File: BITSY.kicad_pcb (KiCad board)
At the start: 4 copper layers, 102 x 102 mm, 64 parts, among them CON1 AudioJack3_SwitchTR, J1 Barrel_Jack_Switch, J2 Conn_01x06, J3 Conn_01x05, J4 Conn_02x22_Odd_Even, J5 Conn_01x40_Pin, J6 Conn_01x01_Socket, J7 Conn_01x01_Socket, J8 Conn_01x01_Socket, J9 Conn_01x01_Socket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

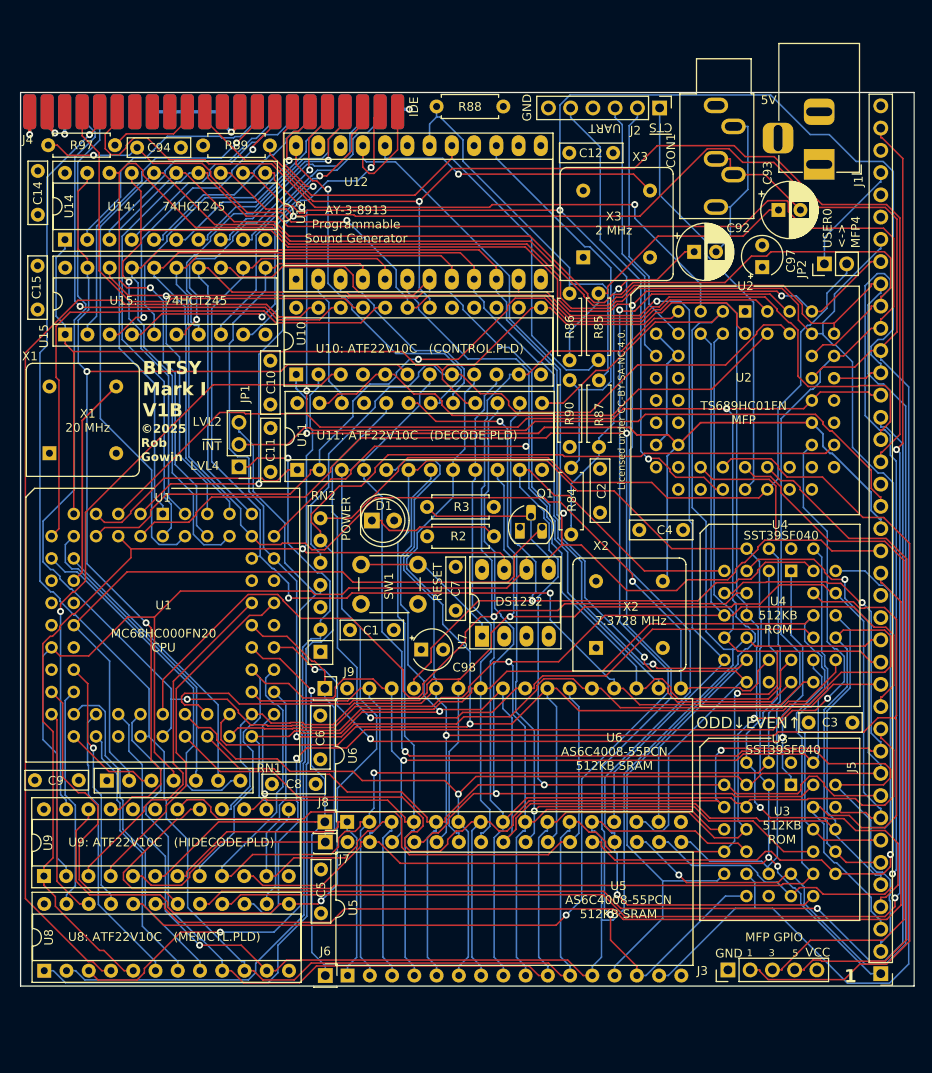
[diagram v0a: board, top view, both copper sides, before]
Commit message: V1C version of BITSY that uses an SRAM SIMM for memory.
This version sent to JLCPCB on 08/15/2025.
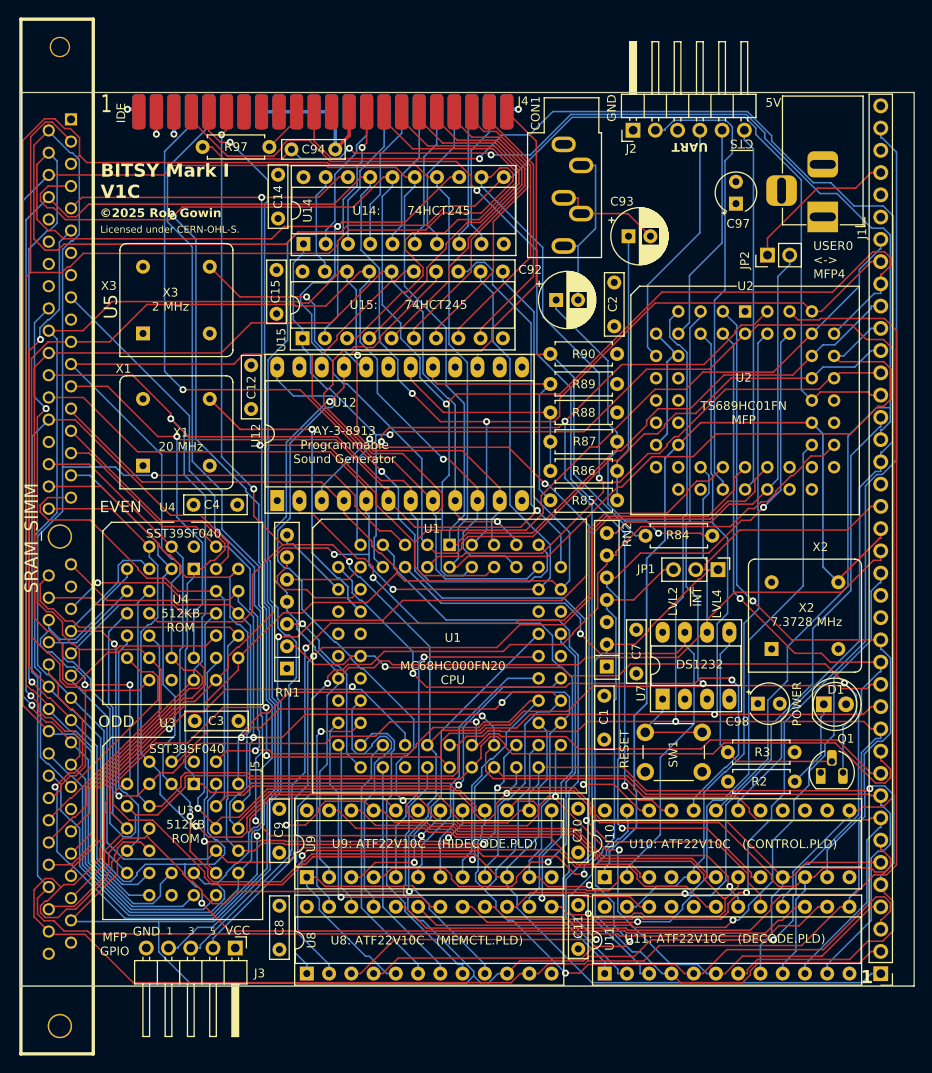
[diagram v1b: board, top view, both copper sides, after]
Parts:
- removed C5, C6: 0.1uF, Capacitor_THT:C_Rect_L7.0mm_W2.0mm_P5.00mm
- removed J6, J7, J8, J9: Conn_01x01_Socket, Connector_PinSocket_2.54mm:PinSocket_1x01_P2.54mm_Vertical
- removed U6: AS6C4008-55PCN, Package_DIP:DIP-32_W15.24mm
- J2: footprint Connector_PinHeader_2.54mm:PinHeader_1x06_P2.54mm_Vertical -> Connector_PinHeader_2.54mm:PinHeader_1x06_P2.54mm_Horizontal
- J3: footprint Connector_PinHeader_2.54mm:PinHeader_1x05_P2.54mm_Vertical -> Connector_PinHeader_2.54mm:PinHeader_1x05_P2.54mm_Horizontal
- U5: value AS6C4008-55PCN -> SRAM_SIMM; footprint Package_DIP:DIP-32_W15.24mm -> SRAM_SIMM:DRAM-72-2021
- moved REF** 71.6 mm to (121.2, 60.7)
- moved C3 70.1 mm to (123.7, 121.2)
- moved U4 68.2 mm to (123.6, 103.8)
- moved U3 68.2 mm to (123.6, 128.4)
- moved U11 67.4 mm to (170.5, 150.0)
- moved U10 67.3 mm to (170.5, 139.0)
- moved C11 64.8 mm to (167.5, 142.2)
- moved U5 59.9 mm to (108.3, 100.1)
- moved C10 58.0 mm to (167.5, 131.2), turned to -90 degrees
- moved J3 56.3 mm to (128.3, 147.1), turned to -90 degrees
- moved C4 56.0 mm to (123.6, 96.5), turned to 0 degrees
- moved JP1 55.9 mm to (183.4, 103.9), turned to -90 degrees
- moved D1 55.7 mm to (195.5, 119.3)
- moved X3 51.0 mm to (117.8, 76.9)
- moved C12 46.6 mm to (130.1, 85.6), turned to 90 degrees
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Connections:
- J2 pad 1: /MFP/~{CTS} -> GND
- J2 pad 2: /MFP/TX -> /MFP/~{RTS}
- J2 pad 3: /MFP/RX -> unconnected-(J2-Pin_3-Pad3)
- J2 pad 4: unconnected-(J2-Pin_4-Pad4) -> /MFP/RX
- J2 pad 5: /MFP/~{RTS} -> /MFP/TX
- J2 pad 6: GND -> /MFP/~{CTS}
- J3 pad 1: GND -> VCC
- J3 pad 2: /MFP/IO1 -> /MFP/IO5
- J3 pad 4: /MFP/IO5 -> /MFP/IO1
- J3 pad 5: VCC -> GND
- U11 pad 19: /~{RDODD} -> /~{READ}
- U11 pad 20: /~{RDEVEN} -> unconnected-(U11-IO3-Pad20)
- U3 pad 24: /~{RDODD} -> /~{READ}
- U4 pad 24: /~{RDEVEN} -> /~{READ}
- U5 pad 1: /A19 -> GND
- U5 pad 10: /A3 -> VCC
- U5 pad 11: /A2 -> /~{WRODD}
- U5 pad 12: /A1 -> unconnected-(U5-A23-Pad12)
- U5 pad 13: /D0 -> unconnected-(U5-A22-Pad13)
- U5 pad 14: /D1 -> unconnected-(U5-A21-Pad14)
- U5 pad 15: /D2 -> unconnected-(U5-A20-Pad15)
- U5 pad 16: GND -> unconnected-(U5-A19-Pad16)
- U5 pad 17: /D3 -> /~{RAM0CS}
- U5 pad 18: /D4 -> /~{READ}
- U5 pad 19: /D5 -> GND
- U5 pad 2: /A17 -> /D0
- U5 pad 20: /D6 -> /D8
- U5 pad 21: /D7 -> /D9
- U5 pad 22: /~{RAMCS} -> /D10
- U5 pad 23: /A11 -> /D11
- U5 pad 24: /~{RDODD} -> /D12
- U5 pad 25: /A12 -> /D13
- U5 pad 26: /A10 -> /D14
- U5 pad 27: /A9 -> /D15
- U5 pad 28: /A14 -> /~{WREVEN}
- U5 pad 29: /~{WRODD} -> /A19
- U5 pad 3: /A15 -> /D1
- U5 pad 30: /A18 -> VCC
- U5 pad 31: /A16 -> /A18
- U5 pad 32: VCC -> /A17
- U5 pad 4: /A13 -> /D2
- U5 pad 5: /A8 -> /D3
- U5 pad 6: /A7 -> /D4
- U5 pad 7: /A6 -> /D5
- U5 pad 8: /A5 -> /D6
- U5 pad 9: /A4 -> /D7
- U9 pad 18: /~{RAMCS} -> /~{RAM0CS}
- U9 pad 20: unconnected-(U9-IO3-Pad20) -> /~{RAM1CS}
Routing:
- net /~{READ}: track 0.00 -> 158.5 mm, vias 0 -> 1
- net /~{WREVEN}: track 78.1 -> 181.0 mm, vias 1 -> 0
- net /~{RDEVEN}: track 95.7 -> 0.00 mm, vias 1 -> 0
- net /~{RDODD}: track 95.6 -> 0.00 mm, vias 2 -> 0
- net /~{RAM0CS}: track 0.00 -> 92.7 mm, vias 0 -> 2
- net /~{WRODD}: track 96.4 -> 180.3 mm, vias 1 -> 2
- net /~{RAM1CS}: track 0.00 -> 77.8 mm, vias 0 -> 2
- net /A2: track 272.0 -> 346.8 mm, vias 2 -> 3
- net /PSGBC1: track 23.9 -> 97.5 mm, vias 0 -> 3
- net /D0: track 208.1 -> 281.3 mm, vias 3 -> 1
- net /~{RAMCS}: track 69.7 -> 0.00 mm
- net /~{IDECS1}: track 51.1 -> 120.5 mm, vias 0 -> 2
- net /~{PSGCS}: track 43.1 -> 111.4 mm, vias 1 -> 2
- net /~{IDECS3}: track 55.0 -> 122.8 mm, vias 1 -> 3
- net /CONTROL/PSGBDIR: track 15.3 -> 82.2 mm, vias 0 -> 2
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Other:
- board text added: "BITSY Mark I MC68HC000 Single Board Computer PCB V1C August 2025 © 2025 Rob Gowin. Licensed under CERN-OHL-S github.com/codesmythe/BITSY_MK_I"
- board text added: "BITSY Mark I V1C"
- board text added: "EVEN"
- board text added: "Licensed under CERN-OHL-S."
- board text added: "ODD"
- board text removed: "BITSY Mark I MC68HC000 Single Board Computer PCB V1B April 2025 © 2025 Rob Gowin. Licensed under CC-BY-SA-NC 4.0. github.com/codesmythe/BITSY_MK_I"
- board text removed: "BITSY Mark I V1B"
- board text removed: "Licensed under CC-BY-SA-NC 4.0."
- board text removed: "ODD↓EVEN↑"
- board text removed: "U5 AS6C4008-55PCN 512KB SRAM"
- board text removed: "U6 AS6C4008-55PCN 512KB SRAM"

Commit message: Add two extra SIMM address lines.
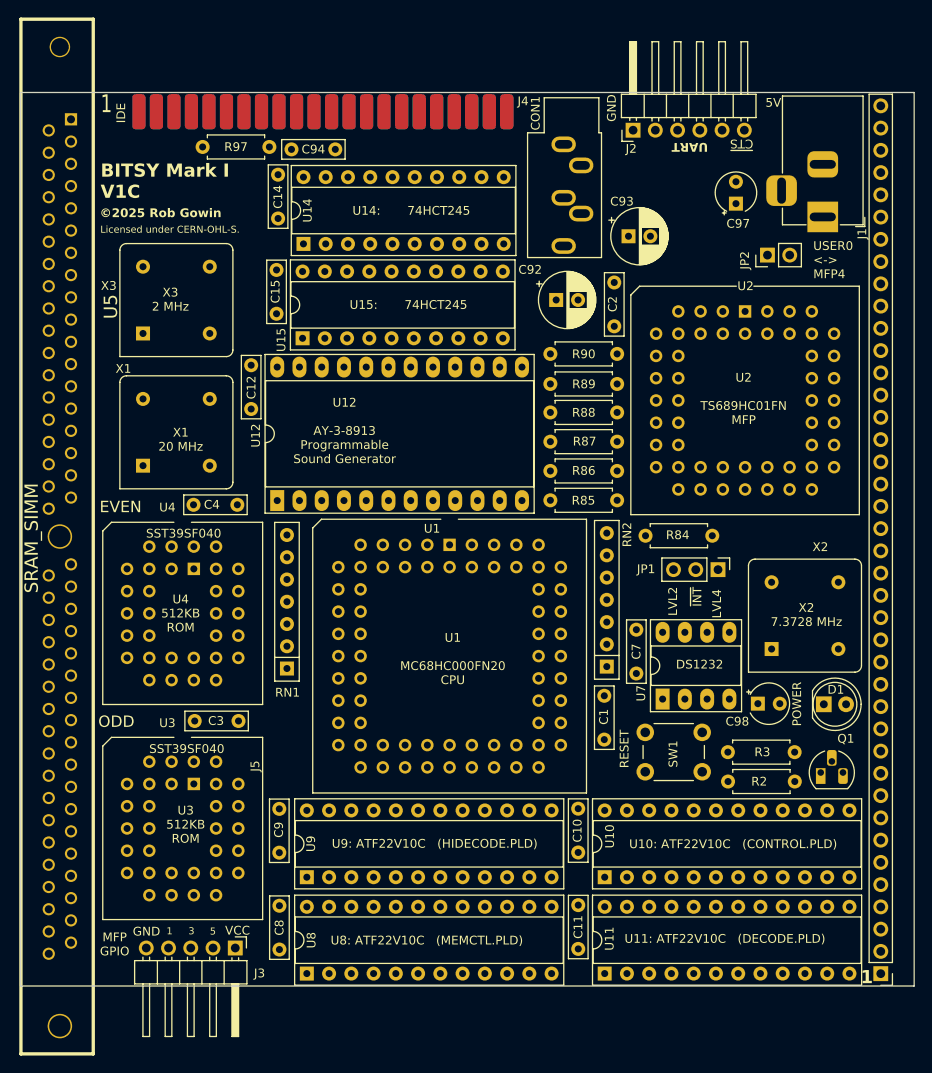
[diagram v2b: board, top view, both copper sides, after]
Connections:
- U5 pad 15: unconnected-(U5-A20-Pad15) -> /A21
- U5 pad 16: unconnected-(U5-A19-Pad16) -> /A20
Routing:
- net /A2: track 346.8 -> 0.00 mm, vias 3 -> 0
- net /D5: track 293.4 -> 0.00 mm, vias 2 -> 0
- net /A3: track 289.6 -> 0.00 mm, vias 5 -> 0
- net /D0: track 281.3 -> 0.00 mm, vias 1 -> 0
- net /A1: track 281.3 -> 0.00 mm, vias 3 -> 0
- net /D3: track 276.3 -> 0.00 mm
- net /D1: track 267.9 -> 0.00 mm, vias 1 -> 0
- net /A4: track 264.5 -> 0.00 mm, vias 3 -> 0
- net /D2: track 261.5 -> 0.00 mm, vias 2 -> 0
- net /D7: track 255.0 -> 0.00 mm, vias 2 -> 0
- net /D4: track 247.8 -> 0.00 mm, vias 1 -> 0
- net /D6: track 245.7 -> 0.00 mm, vias 3 -> 0
- net /~{RESET}: track 204.4 -> 0.00 mm, vias 1 -> 0
- net /A5: track 195.6 -> 0.00 mm, vias 1 -> 0
- net /~{WREVEN}: track 181.0 -> 0.00 mm
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
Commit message: Update version info
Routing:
- net /A2: track 0.00 -> 334.7 mm, vias 0 -> 2
- net /A3: track 0.00 -> 332.6 mm, vias 0 -> 2
- net /D4: track 0.00 -> 289.1 mm, vias 0 -> 2
- net /A1: track 0.00 -> 276.4 mm, vias 0 -> 1
- net /D7: track 0.00 -> 274.7 mm, vias 0 -> 2
- net /D1: track 0.00 -> 269.2 mm, vias 0 -> 2
- net /A4: track 0.00 -> 268.8 mm, vias 0 -> 4
- net /D3: track 0.00 -> 259.6 mm
- net /D2: track 0.00 -> 255.5 mm, vias 0 -> 4
- net /D0: track 0.00 -> 254.9 mm, vias 0 -> 2
- net /D6: track 0.00 -> 254.7 mm
- net /D5: track 0.00 -> 242.9 mm, vias 0 -> 2
- net /~{RESET}: track 0.00 -> 235.8 mm, vias 0 -> 1
- net /A5: track 0.00 -> 217.4 mm, vias 0 -> 4
- net /D13: track 0.00 -> 208.7 mm, vias 0 -> 2
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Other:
- board text added: "BITSY Mark I MC68HC000 Single Board Computer PCB V1D September 2025 © 2025 Rob Gowin. Licensed under CERN-OHL-S github.com/codesmythe/BITSY_MK_I"
- board text added: "BITSY Mark I V1D"
- board text removed: "BITSY Mark I MC68HC000 Single Board Computer PCB V1C August 2025 © 2025 Rob Gowin. Licensed under CERN-OHL-S github.com/codesmythe/BITSY_MK_I"
- board text removed: "BITSY Mark I V1C"

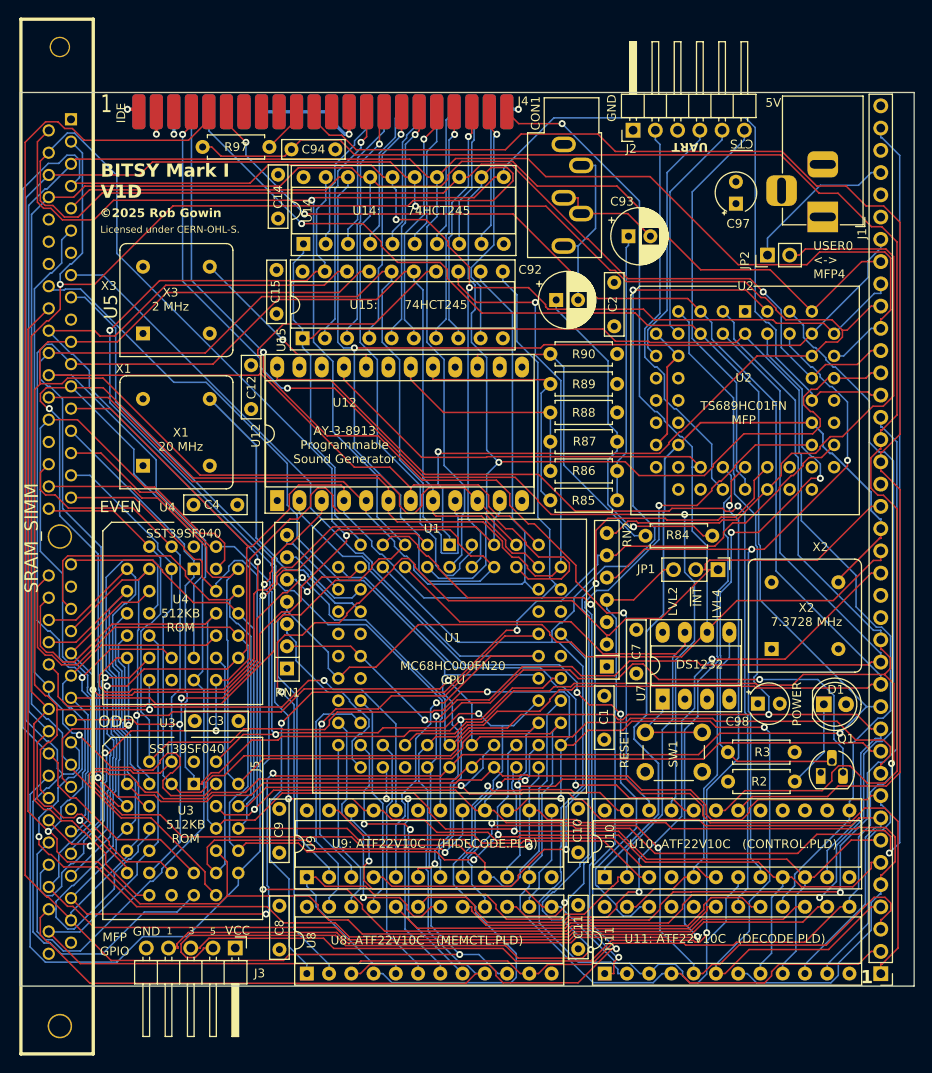
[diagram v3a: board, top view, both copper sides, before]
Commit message: Create V1E version.
Adds extra address line to SIMM for 16 MB support.
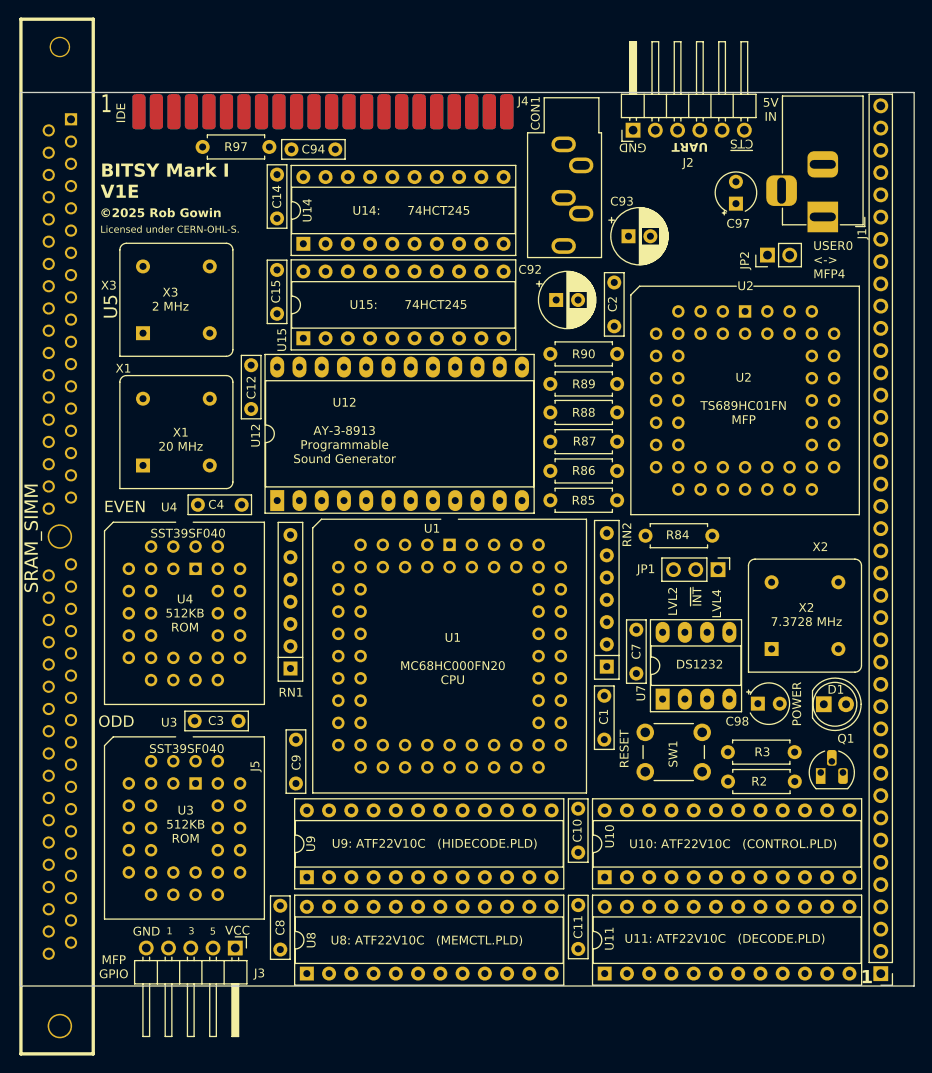
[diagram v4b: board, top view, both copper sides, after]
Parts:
- moved C9 3.47 mm to (135.3, 128.3), turned to 90 degrees
- moved C4 0.50 mm to (124.1, 96.5)
- moved RN1 0.40 mm to (134.6, 115.2)
- moved U3 0.21 mm to (123.8, 128.3)
- moved U4 0.20 mm to (123.8, 103.8)
- moved C14 0.12 mm to (133.1, 58.8)
- moved C8 0.10 mm to (133.5, 142.3)
- moved U15 0.09 mm to (136.1, 77.5)
- moved C15 0.06 mm to (133.1, 69.7)
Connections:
- U5 pad 14: unconnected-(U5-A21-Pad14) -> /A22
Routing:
- net /A2: track 334.7 -> 0.00 mm, vias 2 -> 0
- net /A3: track 332.6 -> 0.00 mm, vias 2 -> 0
- net /D4: track 289.1 -> 0.00 mm, vias 2 -> 0
- net /A1: track 276.4 -> 0.00 mm, vias 1 -> 0
- net /D7: track 274.7 -> 0.00 mm, vias 2 -> 0
- net /D1: track 269.2 -> 0.00 mm, vias 2 -> 0
- net /A4: track 268.8 -> 0.00 mm, vias 4 -> 0
- net /D3: track 259.6 -> 0.00 mm
- net /D2: track 255.5 -> 0.00 mm, vias 4 -> 0
- net /D0: track 254.9 -> 0.00 mm, vias 2 -> 0
- net /D6: track 254.7 -> 0.00 mm
- net /D5: track 242.9 -> 0.00 mm, vias 2 -> 0
- net /~{RESET}: track 235.8 -> 0.00 mm, vias 1 -> 0
- net /A5: track 217.4 -> 0.00 mm, vias 4 -> 0
- net /D13: track 208.7 -> 0.00 mm, vias 2 -> 0
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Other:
- board text added: "5V IN"
- board text added: "BITSY Mark I MC68HC000 Single Board Computer PCB V1E November 2025 © 2025 Rob Gowin. Licensed under CERN-OHL-S github.com/codesmythe/BITSY_MK_I"
- board text added: "BITSY Mark I V1E"
- board text removed: "5V"
- board text removed: "BITSY Mark I MC68HC000 Single Board Computer PCB V1D September 2025 © 2025 Rob Gowin. Licensed under CERN-OHL-S github.com/codesmythe/BITSY_MK_I"
- board text removed: "BITSY Mark I V1D"
